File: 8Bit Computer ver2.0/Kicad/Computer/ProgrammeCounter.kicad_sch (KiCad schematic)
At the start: 10 parts, among them IC65 SN74HCS4075DR, IC66 SN74LVC1G32DBVR, IC67 SN74LVC1G32DBVR, IC68 SN74LVC1G08DBVR, IC69 CY74FCT163CTSOC, IC70 CY74FCT163CTSOC, IC71 CY74FCT163CTSOC, IC72 CY74FCT163CTSOC, IC73 SN74LVC1G14DBVR, IC74 SN74LVC1G14DBVR

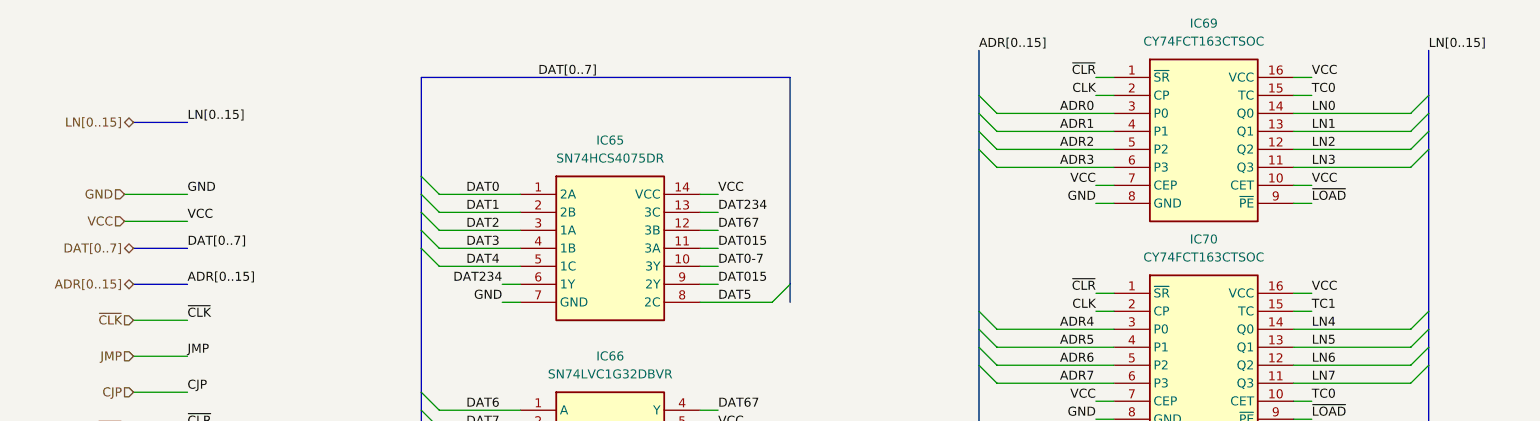
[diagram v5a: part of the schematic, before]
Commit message: Kicad,parts
Kicad:
worked on Flash memory
began RAM
parts:
added Delay Chip for Flash
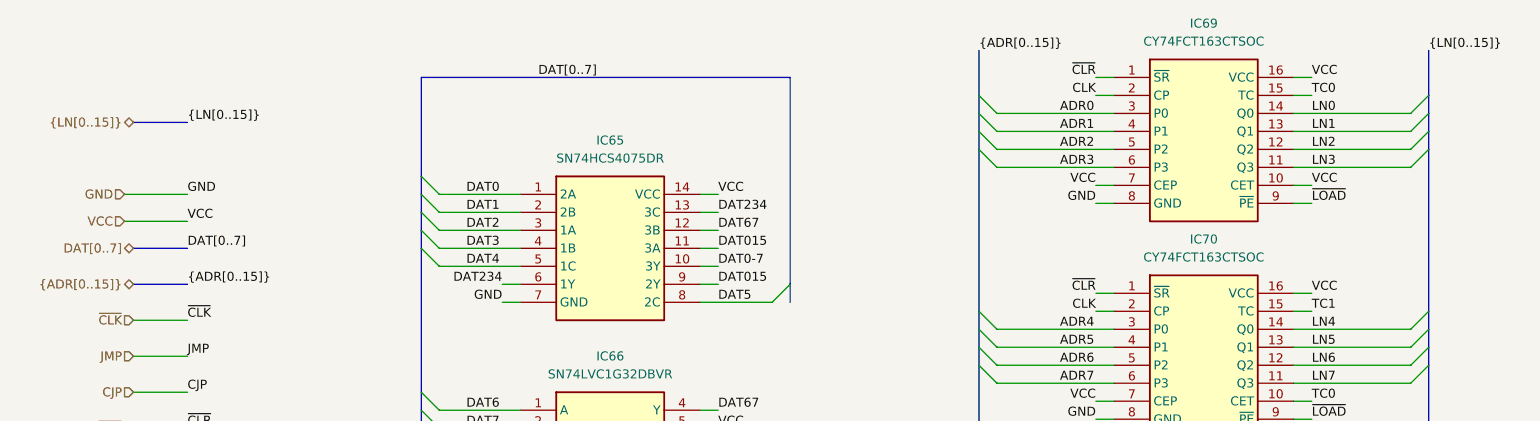
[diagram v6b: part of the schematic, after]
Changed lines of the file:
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@@
 			"UUVnQUFBQUFBQUFBQUFBd0FBQUFBQUFBRHdYMVQrMVFFQUFBRUFBQUFBQUFBQUFBQUFBQUFBQUFD"
 			"RmU5UmdBRlVFZ0NEd1UvN1ZBUUFBQXdBQUFBQUFBQUNBb0ZUKzFRRUFBQUVBQUFBQUFBQUFBQUFB"
-			"QUFBQUFBQ0dlOHRnQUZZRWdBQUFBQUFBQUFBQUJBQQ=="
+			"QUFBQUFBQ0dlOHRnQUZZRWdBQUFBQUFBQUFBQUJBQQAAAAAAAAAAAAAAAAAAAAAAAAAAAAAAAAAA"
+			"AAAAAAAAAAAAAAAAAAAAAAAAAAAAAAAAAAAAAAAAAAAAAAAAAAAAAAAAAAAAAAAAAAAAAAAAAAAA"
+			"AAAAAAAAAAAAAAAAAAAAAAAAAAAAAAAAAAAAAAAAAAAAAAAAAAAAAAAAAAAAAAAAAAAAAAAAAAAA"
+			"AAAAAAAAAAAAAAAAAAAAAAAAAAAAAAAAAAAAAAAAAAAAAAAAAAAAAAAAAAAAAAAAAAAAAAAAAAAA"
+			"AAAAAAAAAAAAAAAAAAAAAAAAAAAAAAAAAAAAAAAAAAAAAAAAAAAAAAAAAAAAAAAAAAAAAAAAAAAA"
+			"AAAAAAAAAAAAAAAAAAAAAAAAAAAAAAAAAAAAAAAAAAAAAAAAAAAAAAAAAAAAAAAAAAAAAAAAAAAA"
+			"AAAAAAAAAAAAAAAAAAAAAAAAAAAAAAAAAAAAAAAAAAAAAAAAAAAAAAAAAAAAAAAAAAAAAAAAAAAA"
+			"AAAAAAAAAAAAAAAAAAAAAAAAAAAAAAAAAAAAAAAAAAAAAAAAAAAAAAAAAAAAAAAAAAAAAAAAAAAA"
+			"AAAAAAAAAAAAAAAAAAAAAAAAAAAAAAAAAAAAAAAAAAAAAAAAAAAAAAAAAAAAAAAAAAAAAAAAAAAA"
+			"AAAAAAAAAAAAAAAAAAAAAAAAAAAAAAAAAAAAAAAAAAAAAAAAAAAAAAAAAAAAAAAAAAAAAAAAAAAA"
+			"AAAAAAAAAAAAAAAAAAAAAAAAAAAAAAAAAAAAAAAAAAAAAAAAAAAAAAAAAAAAAAAAAAAAAAAAAAAA"
+			"AAAAAAAAAAAAAAAAAAAAAAAAAAAAAAAAAAAAAAAAAAAAAAAAAAAAAAAAAAAAAAAAAAAAAAAAAAAA"
+			"AAAAAAAAAAAAAAAAAAAAAAAAAAAAAAAAAAAAAAAAAAAAAAAAAAAAAAAAAAAAAAAAAAAAAAAAAAAA"
+			"AAAAAAAAAAAAAAAAAAAAAAAAAAAAAAAAAAAAAAAAAAAAAAAAAAAAAAAAAAAAAAAAAAAAAAAAAAAA"
+			"AAAAAAAAAAAAAAAAAAAAAAAAAAAAAAAAAAAAAAAAAAAAAAAAAAAAAAAAAAAAAAAAAAAAAAAAAAAA"
+			"AAAAAAAAAAAAAAAAAAAAAAAAAAAAAAAAAAAAAAAAAAAAAAAAAAAAAAAAAAAAAAAAAAAAAAAAAAAA"
+			"AAAAAAAAAAAAAAAAAAAAAAAAAAAAAAAAAAAAAAAAAAAAAAAAAAAAAAAAAAAAAAAAAAAAAAAAAAAA"
+			"AAAAAAAAAAAAAAAAAAAAAAAAAAAAAAAAAAAAAAAAAAAAAAAAAAAAAAAAAAAAAAAAAAAAAAAAAAAA"
+			"AAAAAAAAAAAAAAAAAAAAAAAAAAAAAAAAAAAAAAAAAA=="
 		)
 	)
@@
 		)
 	)
-	(label "LN[0..15]"
+	(label "{LN[0..15]}"
 		(at 218.44 29.21 0)
 		(effects
@@
 		)
 	)
-	(label "ADR[0..15]"
+	(label "{ADR[0..15]}"
 		(at 154.94 29.21 0)
 		(effects
@@
 		)
 	)
-	(label "LN[0..15]"
+	(label "{LN[0..15]}"
 		(at 43.18 39.37 0)
 		(effects
@@
 		)
 	)
-	(label "ADR[0..15]"
+	(label "{ADR[0..15]}"
 		(at 43.18 62.23 0)
 		(effects
@@
 		)
 	)
-	(hierarchical_label "ADR[0..15]"
+	(hierarchical_label "{ADR[0..15]}"
 		(shape tri_state)
 		(at 35.56 62.23 180)
@@
 		)
 	)
-	(hierarchical_label "LN[0..15]"
+	(hierarchical_label "{LN[0..15]}"
 		(shape tri_state)
 		(at 35.56 39.37 180)

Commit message: Kicad, parts
parts:
added USB C PD Triggerboard
added Delay Chip for 90ns
added Push Button
Kicad:
added USB C PD Triggerboard
added rising edge detector via Delay and Xor for Accept Push Button
added VBUS net
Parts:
- added IC182, IC183: SN74F521DWR, Samacsys:SOIC127P1030X265-20N, symbol Samacsys:SN74F521DWR
- added IC184, IC185: SN74LVC1G14DBVR, Samacsys:SOT95P280X145-5N, symbol Samacsys:SN74LVC1G14DBVR
- added R40: 4.7k, Resistor_SMD:R_1206_3216Metric_Pad1.30x1.75mm_HandSolder, symbol Device:R
- added S9: B3FS-4055P, Samacsys:B3FS4055P, symbol Samacsys:B3FS-4055P
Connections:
- net CJP: now also IC185.4 (Y)
- net GND: now also IC182.1 (~{OE}), IC182.10 (GND), IC182.12 (Q4), IC182.14 (Q5), IC182.16 (Q6), IC182.18 (Q7), IC182.5 (Q1), IC182.7 (Q2), IC182.9 (Q3), IC183.1 (~{OE}), IC183.10 (GND), IC183.12 (Q4), IC183.14 (Q5), IC183.16 (Q6), IC183.18 (Q7), IC183.3 (Q0), IC183.7 (Q2), IC183.9 (Q3), IC184.3 (GND), IC185.3 (GND), S9.1 (COM_1), S9.2 (COM_2)
- net JMP: now also IC184.4 (Y)
- net VCC: now also IC182.20 (VCC), IC182.3 (Q0), IC183.20 (VCC), IC183.5 (Q1), IC184.5 (VCC), IC185.5 (VCC), R40.2
- net ~{CLR}: now also R40.1, S9.3 (NO_1), S9.4 (NO_2)
- new net: IC183.19 (~{P_=_Q}), IC185.2 (A)
- new net: IC182.19 (~{P_=_Q}), IC184.2 (A)
- new net CMD0: IC182.2 (P0), IC183.2 (P0)
- new net CMD1: IC182.4 (P1), IC183.4 (P1)
- new net CMD2: IC182.6 (P2), IC183.6 (P2)
- new net CMD3: IC182.8 (P3), IC183.8 (P3)
- new net CMD4: IC182.11 (P4), IC183.11 (P4)
- new net CMD5: IC182.13 (P5), IC183.13 (P5)
- new net CMD6: IC182.15 (P6), IC183.15 (P6)
- new net CMD7: IC182.17 (P7), IC183.17 (P7)
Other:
- note added: "0000 0001"
- note added: "0000 0010"
- note added: "0x01"
- note added: "0x02"
- note added: "CLEAR Button"
- moved on the sheet: IC65, IC66, IC67, IC68, IC69, IC70, IC71, IC72, IC73, IC74

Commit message: Kicad
changed to module version
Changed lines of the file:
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@@
 		)
 	)
-	(wire
-		(pts
-			(xy 238.76 217.17) (xy 241.3 217.17)
-		)
-		(stroke
-			(width 0)
-			(type default)
-		)
-	)
 	(bus
 		(pts
@@
 	(wire
 		(pts
+			(xy 238.76 217.17) (xy 241.3 217.17)
+		)
+		(stroke
+			(width 0)
+			(type default)
+		)
+	)
+	(wire
+		(pts
 			(xy 100.33 132.08) (xy 102.87 132.08)
 		)
@@
 		)
 	)
-	(label "VCC"
-		(at 241.3 217.17 0)
-		(effects
-			(font
-				(size 1.27 1.27)
-			)
-			(justify left bottom)
-		)
-	)
 	(label "~{CLR}"
 		(at 341.63 186.69 180)
@@
 		)
 	)
-	(label "{LN[0..15]}"
+	(label "LN[0..15]"
 		(at 388.62 121.92 0)
 		(effects
@@
 		)
 	)
-	(label "{ADR[0..15]}"
+	(label "ADR[0..15]"
 		(at 325.12 121.92 0)
 		(effects
@@
 		)
 	)
-	(label "{LN[0..15]}"
+	(label "LN[0..15]"
 		(at 39.37 64.77 0)
 		(effects
@@
 		)
 	)
-	(label "{ADR[0..15]}"
+	(label "ADR[0..15]"
 		(at 39.37 87.63 0)
 		(effects
@@
 		)
 	)
+	(label "VCC"
+		(at 241.3 217.17 0)
+		(effects
+			(font
+				(size 1.27 1.27)
+			)
+			(justify left bottom)
+		)
+	)
 	(label "GND"
 		(at 152.4 113.03 0)
@@
 		)
 	)
-	(hierarchical_label "{ADR[0..15]}"
+	(hierarchical_label "ADR[0..15]"
 		(shape tri_state)
 		(at 31.75 87.63 180)
@@
 		)
 	)
-	(hierarchical_label "{LN[0..15]}"
+	(hierarchical_label "LN[0..15]"
 		(shape tri_state)
 		(at 31.75 64.77 180)
